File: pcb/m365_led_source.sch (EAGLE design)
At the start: 36 parts, among them M1 BSC037N08NS5ATMA1, M2 CSD19534Q5A

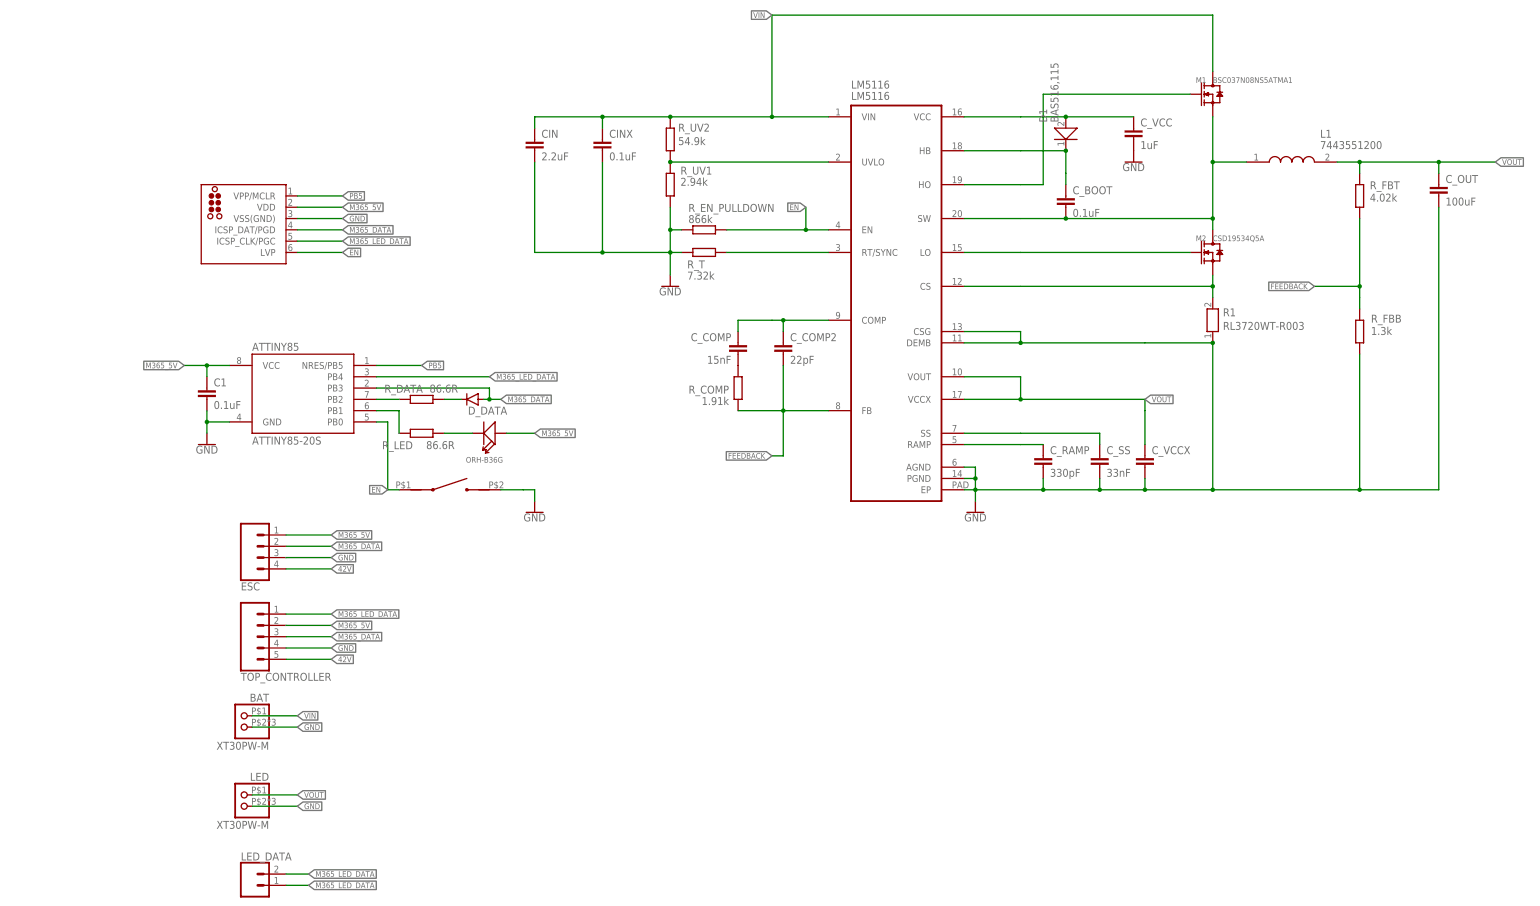
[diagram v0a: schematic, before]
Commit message: Updated led source board. Added RTC chip + regulator for it Changed the pinout of the attiny45 so that it can be programmed in place
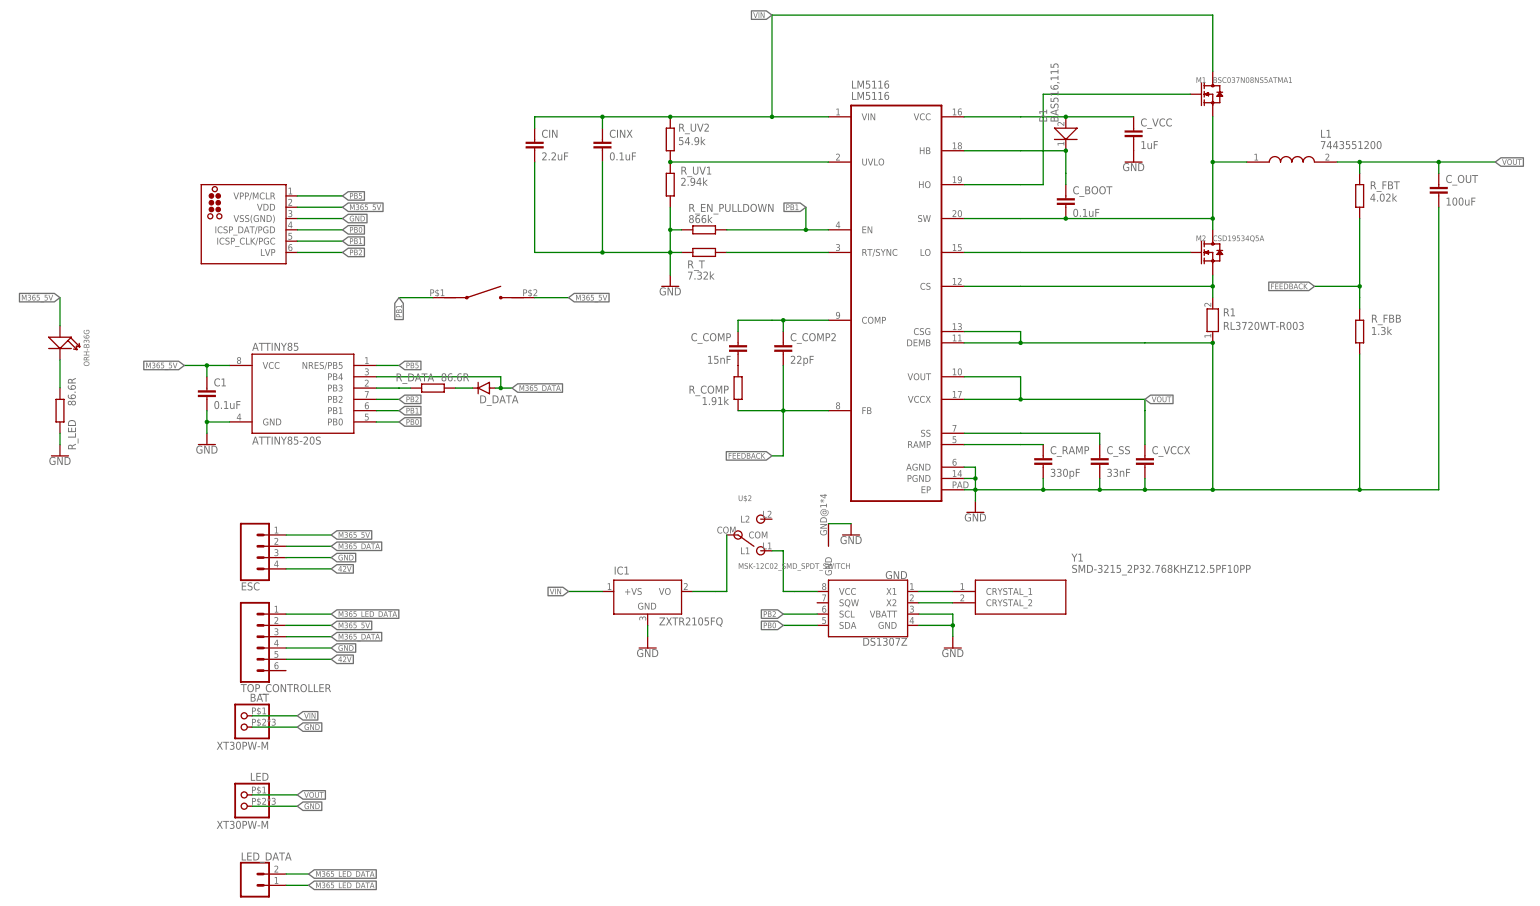
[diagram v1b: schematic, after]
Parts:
- added GND: DS1307Z, SparkFun-Clocks:DS1307Z
- added IC1: ZXTR2105FQ, linear:LM50
- added U$2: MSK-12C02_SMD_SPDT_SWITCH, MSK-12C02 SMD Micro Slider Switch SPDT:MSK-12C02_SMD_SPDT_SWITCH
- added Y1: SMD-3215_2P32.768KHZ12.5PF10PP, SMD-3215_2P32.768KHZ12.5PF10PP:SMD-3215_2P32.768KHZ12.5PF10PP
- TOP_CONTROLLER: device SparkFun-Connectors:CONN_05PTH_LONGPADS -> SparkFun-Connectors:CONN_06LONGPADS
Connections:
- removed net EN: ATTINY85.PB0, J2.LVP, LM5116.EN, R_EN_PULLDOWN.2, U$1.P$1
- new net 5V_REG: IC1.VO, U$2.COM
- new net N$11: GND.X2, Y1.CRYSTAL_2
- new net N$6: GND.X1, Y1.CRYSTAL_1
- new net PB0: ATTINY85.PB0, GND.SDA, J2.ICSP_DAT/PGD
- new net PB1: ATTINY85.PB1, J2.ICSP_CLK/PGC, LM5116.EN, R_EN_PULLDOWN.2, U$1.P$1
- new net PB3: ATTINY85.PB3, R_DATA.1
- net GND: now also GND.GND, GND.VBATT, IC1.GND, R_LED.1, U$2.GND; no longer U$1.P$2
- net M365_5V: now also U$1.P$2
- net M365_DATA: now also ATTINY85.PB4; no longer ATTINY85.PB3, J2.ICSP_DAT/PGD
- net M365_LED_DATA: no longer ATTINY85.PB4, J2.ICSP_CLK/PGC
- net N$3: now also GND.VCC, U$2.L1; no longer ATTINY85.PB1, R_LED.1
- net PB2: now also GND.SCL, J2.LVP; no longer R_DATA.1
- net VIN: now also IC1.+VS
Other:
- moved on the sheet: D_DATA, R_DATA, R_LED
